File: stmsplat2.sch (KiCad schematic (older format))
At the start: 97 parts, among them J1 C11_2X36, J10 Conn_01x03_Male, J11 Conn_01x02_Male, J12 Conn_01x04_Male, J13 Conn_01x04_Male, J14 Conn_01x02, J15 Conn_01x02, J16 Screw_Terminal_01x03, J17 Screw_Terminal_01x02, J2 C12_2X36, J3 Conn_01x04_Male, J4 Conn_01x04_Male, J5 Conn_Coaxial, J6 Conn_01x06, J7 Conn_01x04_Male, J8 Conn_01x04_Male, J9 Conn_01x03_Male, Q1 BSS138LT1G, U1 ublox_chinese_PCB_module, U10 XCVR_E30-400M20S, U2 ESP-C3-13U, U3 SST25VF032B, U4 48L512-48LM01, U5 Opamp_Quad_MCP6024, U6 E180-ZG120A, U7 AZ1084C, U8 MCP6S93-X_UN, U9 DS2485

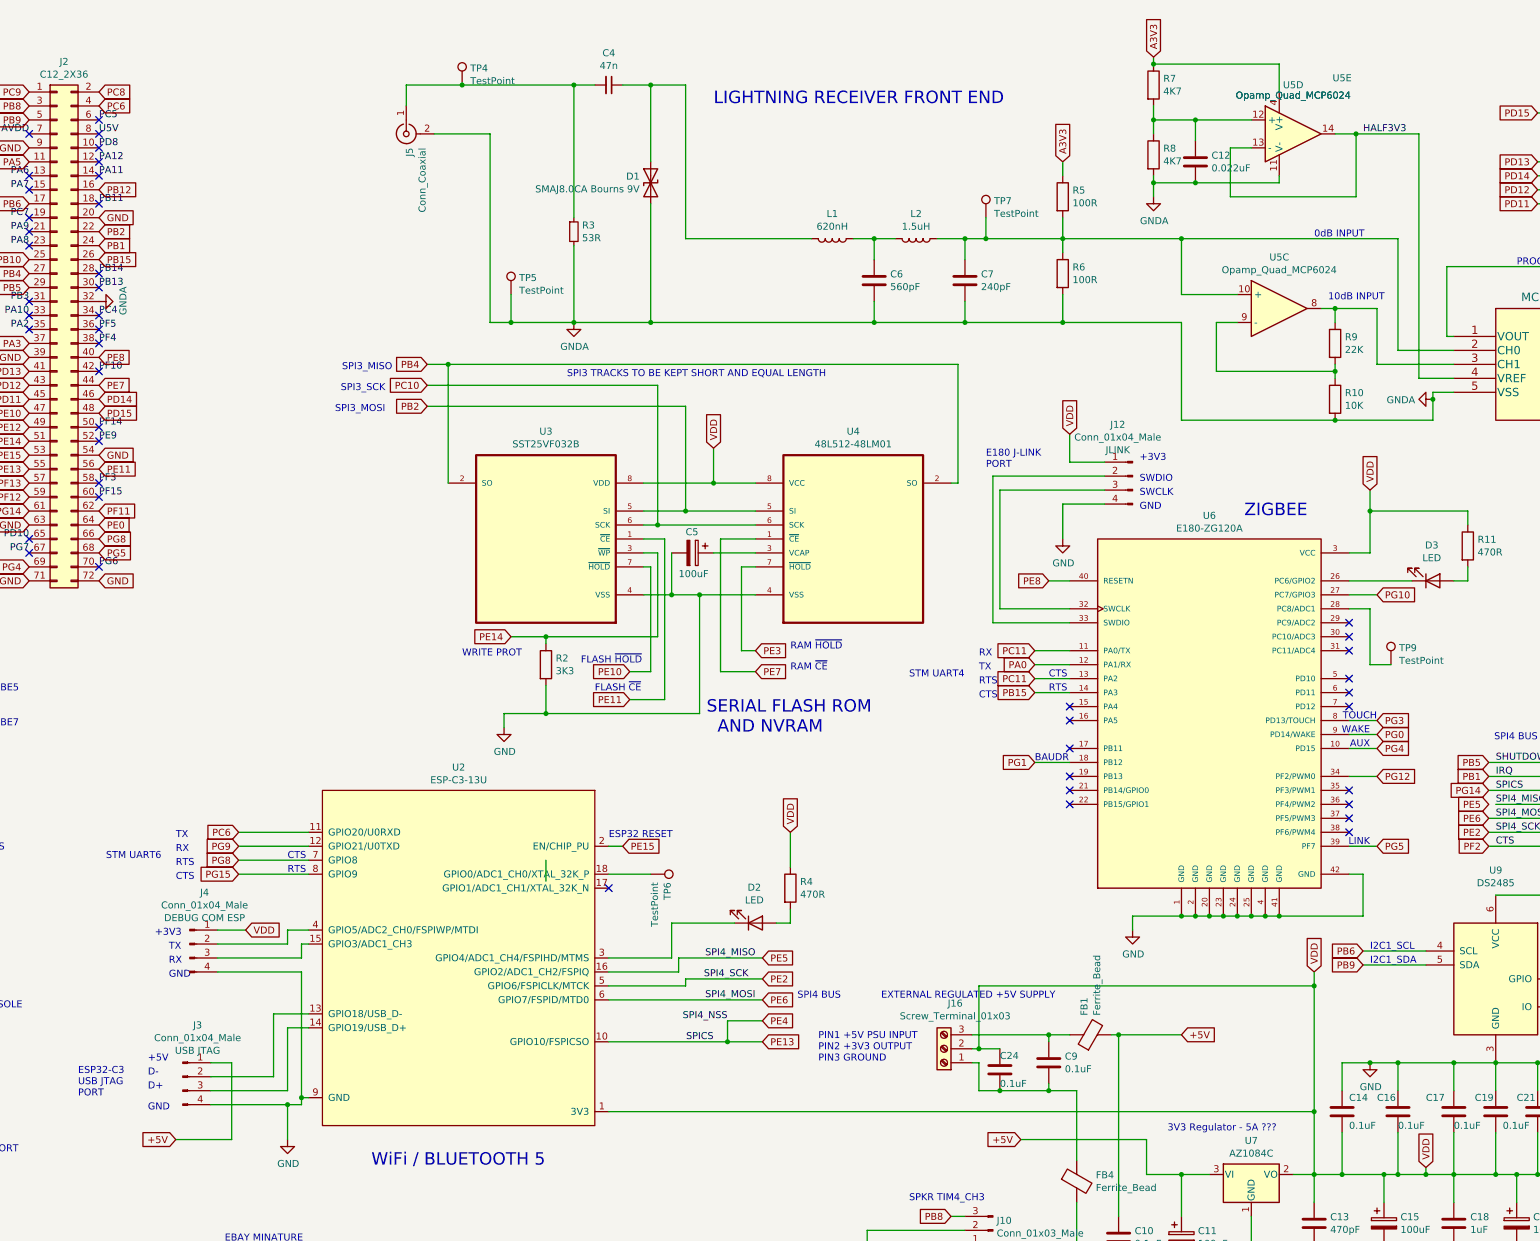
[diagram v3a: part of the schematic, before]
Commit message: 0 ERC - modified custom lib to clarify pin types
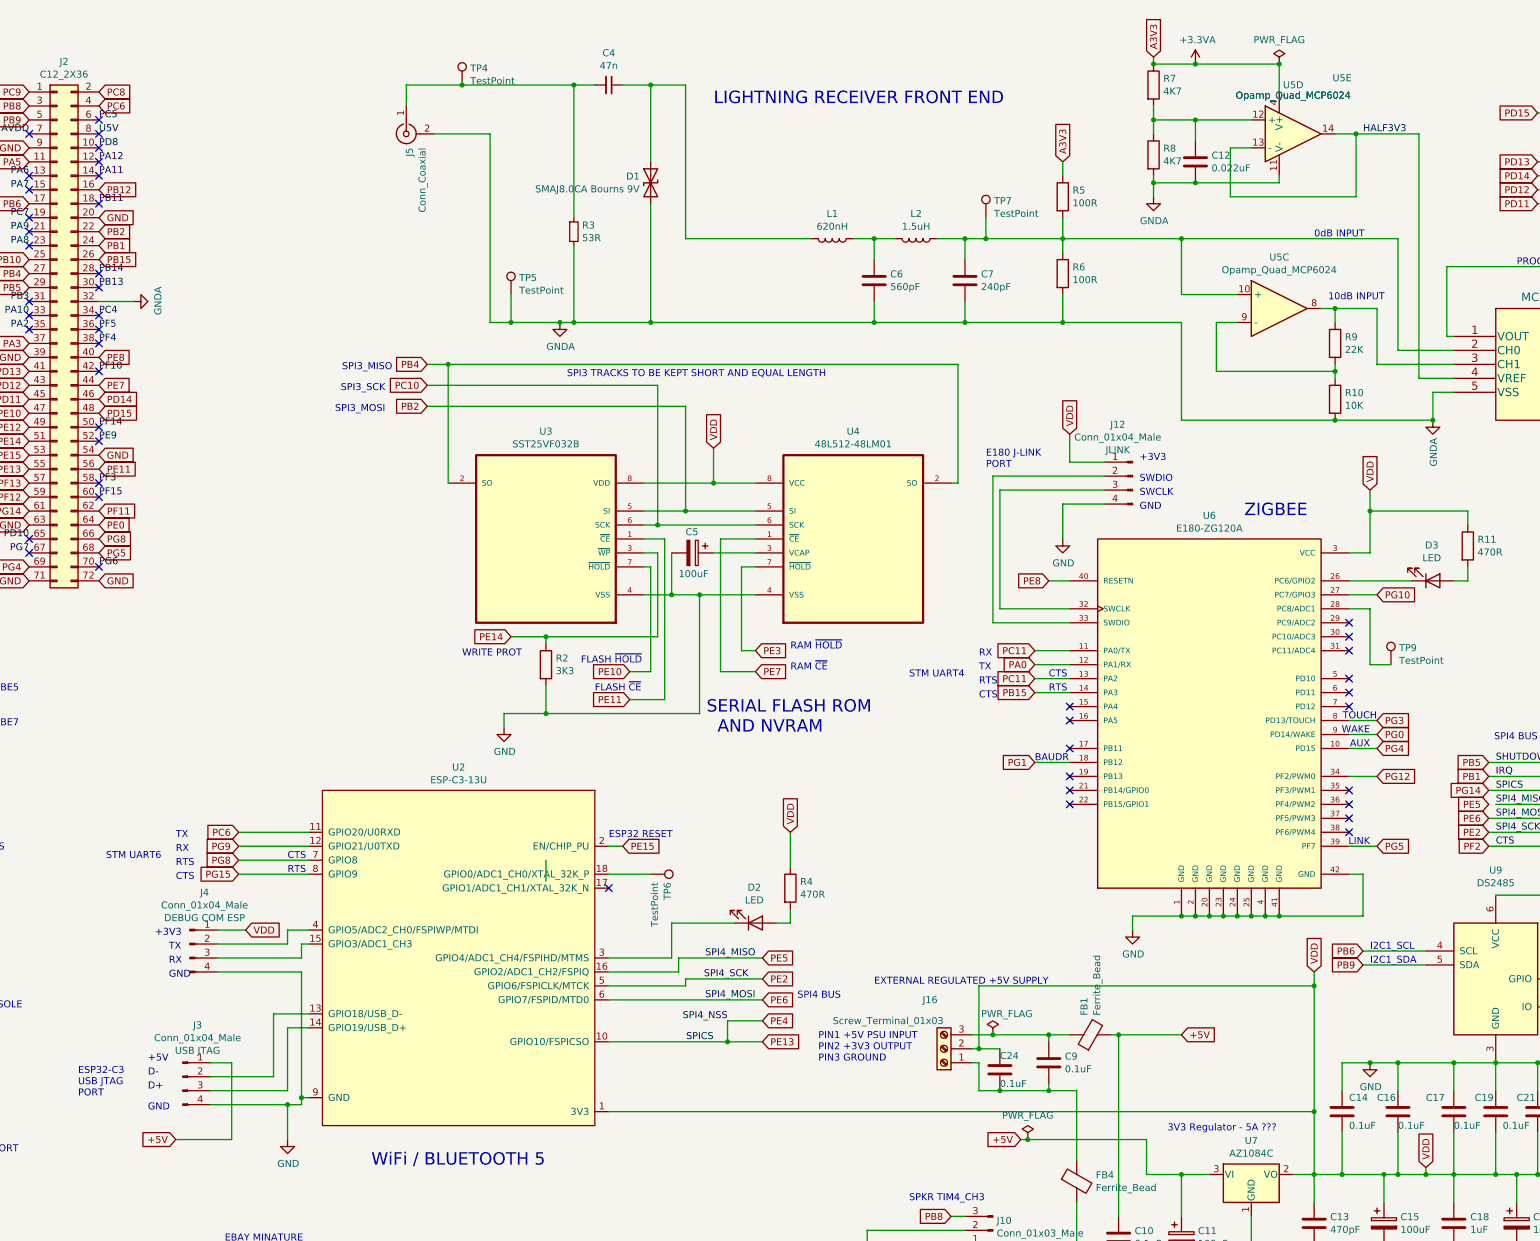
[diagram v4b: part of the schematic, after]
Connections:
- net A3V3 renamed +3.3VA
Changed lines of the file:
@@
 Connection ~ 6950 2650
-Wire Wire Line
-	6400 2650 6950 2650
-Connection ~ 6400 2650
 Wire Wire Line
 	6400 950  6400 1900
@@
 Connection ~ 5950 2650
 Wire Wire Line
-	5950 2650 6400 2650
+	5950 2650 6300 2650
 Wire Wire Line
 	12700 3150 12550 3150
@@
 Wire Wire Line
 	11250 9050 11250 9450
-Text Notes 8600 7500 0    50   ~ 0
+Text Notes 8550 7400 0    50   ~ 0
 EXTERNAL REGULATED +5V SUPPLY
 $Comp
@@
 $EndComp
 Wire Wire Line
-	10550 800  11450 800
+	10550 800  10850 800
 Wire Wire Line
 	11450 800  11450 1000
@@
 U 1 1 622C2AE8
 P 9050 7850
-F 0 "J16" H 8970 7525 50  0000 C CNN
-F 1 "Screw_Terminal_01x03" H 8970 7616 50  0000 C CNN
+F 0 "J16" H 9150 7500 50  0000 C CNN
+F 1 "Screw_Terminal_01x03" H 9450 7650 50  0000 C CNN
 F 2 "TerminalBlock:TerminalBlock_Altech_AK300-3_P5.00mm" H 9050 7850 50  0001 C CNN
 F 3 "~" H 9050 7850 50  0001 C CNN
@@
 $EndComp
 Wire Wire Line
-	9250 7750 9800 7750
+	9250 7750 9400 7750
 Wire Wire Line
 	9250 7950 9300 7950
@@
 	10300 7750 10750 7750
 Wire Wire Line
-	10500 8500 9600 8500
+	10500 8500 9650 8500
 $Comp
 L Connector:Conn_01x04_Male J13
@@
 L power:GNDA #PWR0106
 U 1 1 6451C4EF
-P 12550 3200
-F 0 "#PWR0106" H 12550 2950 50  0001 C CNN
-F 1 "GNDA" V 12555 3073 50  0000 R CNN
-F 2 "" H 12550 3200 50  0001 C CNN
-F 3 "" H 12550 3200 50  0001 C CNN
-	1    12550 3200
-	0    1    1    0
-$EndComp
-Wire Wire Line
-	12550 3150 12550 3200
-Connection ~ 12550 3200
-Wire Wire Line
-	12550 3200 12550 3350
+P 12550 3350
+F 0 "#PWR0106" H 12550 3100 50  0001 C CNN
+F 1 "GNDA" V 12555 3223 50  0000 R CNN
+F 2 "" H 12550 3350 50  0001 C CNN
+F 3 "" H 12550 3350 50  0001 C CNN
+	1    12550 3350
+	1    0    0    -1
+$EndComp
 $Comp
 L power:GNDA #PWR0107
 U 1 1 6466C53B
-P 6400 2650
-F 0 "#PWR0107" H 6400 2400 50  0001 C CNN
-F 1 "GNDA" H 6405 2477 50  0000 C CNN
-F 2 "" H 6400 2650 50  0001 C CNN
-F 3 "" H 6400 2650 50  0001 C CNN
-	1    6400 2650
+P 6300 2650
+F 0 "#PWR0107" H 6300 2400 50  0001 C CNN
+F 1 "GNDA" H 6305 2477 50  0000 C CNN
+F 2 "" H 6300 2650 50  0001 C CNN
+F 3 "" H 6300 2650 50  0001 C CNN
+	1    6300 2650
 	1    0    0    -1
 $EndComp
@@
 L power:GNDA #PWR0109
 U 1 1 648B7644
-P 3000 2500
-F 0 "#PWR0109" H 3000 2250 50  0001 C CNN
-F 1 "GNDA" H 3005 2327 50  0000 C CNN
-F 2 "" H 3000 2500 50  0001 C CNN
-F 3 "" H 3000 2500 50  0001 C CNN
-	1    3000 2500
+P 3250 2500
+F 0 "#PWR0109" H 3250 2250 50  0001 C CNN
+F 1 "GNDA" H 3255 2327 50  0000 C CNN
+F 2 "" H 3250 2500 50  0001 C CNN
+F 3 "" H 3250 2500 50  0001 C CNN
+	1    3250 2500
 	0    -1   -1   0
 $EndComp
@@
 Text GLabel 1650 1200 2    50   Input ~ 0
 +5V
+$Comp
+L power:PWR_FLAG #FLG0101
+U 1 1 65260660
+P 9400 7750
+F 0 "#FLG0101" H 9400 7825 50  0001 C CNN
+F 1 "PWR_FLAG" H 9500 7900 50  0000 C CNN
+F 2 "" H 9400 7750 50  0001 C CNN
+F 3 "~" H 9400 7750 50  0001 C CNN
+	1    9400 7750
+	1    0    0    -1
+$EndComp
+$Comp
+L power:+3.3VA #PWR0110
+U 1 1 652B4945
+P 10850 800
+F 0 "#PWR0110" H 10850 650 50  0001 C CNN
+F 1 "+3.3VA" H 10865 973 50  0000 C CNN
+F 2 "" H 10850 800 50  0001 C CNN
+F 3 "" H 10850 800 50  0001 C CNN
+	1    10850 800
+	1    0    0    -1
+$EndComp
+Connection ~ 10850 800
+Wire Wire Line
+	10850 800  11450 800
+Connection ~ 9400 7750
+Wire Wire Line
+	9400 7750 9800 7750
+Wire Wire Line
+	3250 2500 3000 2500
+Connection ~ 12550 3350
+Wire Wire Line
+	12550 3150 12550 3350
+Connection ~ 6300 2650
+Wire Wire Line
+	6300 2650 6400 2650
+Connection ~ 6400 2650
+Wire Wire Line
+	6400 2650 6950 2650
+$Comp
+L power:PWR_FLAG #FLG0102
+U 1 1 65603B28
+P 9650 8500
+F 0 "#FLG0102" H 9650 8575 50  0001 C CNN
+F 1 "PWR_FLAG" H 9650 8673 50  0000 C CNN
+F 2 "" H 9650 8500 50  0001 C CNN
+F 3 "~" H 9650 8500 50  0001 C CNN
+	1    9650 8500
+	1    0    0    -1
+$EndComp
+Connection ~ 9650 8500
+Wire Wire Line
+	9650 8500 9600 8500
+$Comp
+L power:PWR_FLAG #FLG0103
+U 1 1 656049AA
+P 11450 800
+F 0 "#FLG0103" H 11450 875 50  0001 C CNN
+F 1 "PWR_FLAG" H 11450 973 50  0000 C CNN
+F 2 "" H 11450 800 50  0001 C CNN
+F 3 "~" H 11450 800 50  0001 C CNN
+	1    11450 800
+	1    0    0    -1
+$EndComp
+Connection ~ 11450 800
 $EndSCHEMATC

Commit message: Rejigged library
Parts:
- U1: symbol stmsplat2-rescue:ublox_SAM-M8Q-splatsyms-stmsplat1-rescue-stmsplat2-rescue -> stmsplat2-custom:ublox_SAM-M8Q
- U10: symbol stmsplat2-rescue:XCVR_E30-400M20S-splatlib -> stmsplat2-custom:XCVR_E30-400M20S
- U2: symbol stmsplat2-rescue:ESP32-C3-13-Espressif -> stmsplat2-custom:ESP32-C3-13-Espressif
- U3: symbol stmsplat2-rescue:SST25VF032B-splatlib -> stmsplat2-custom:SST25VF032B
- U4: symbol stmsplat2-rescue:48L512-48LM01-splatlib -> stmsplat2-custom:48L512-48LM01
- U6: symbol stmsplat2-rescue:E180-ZG120A-splatlib -> stmsplat2-custom:E180-ZG120A
- U7: symbol stmsplat2-rescue:AZ1084C-splatlib -> stmsplat2-custom:AZ1084C
- U8: symbol stmsplat2-rescue:MCP6S93-X_UN-splatsyms -> stmsplat2-custom:MCP6S93-X_UN
- U9: symbol stmsplat2-rescue:DS2485-splatlib -> stmsplat2-custom:DS2485
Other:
- note added: "VER 0.06: ALMOST FROZEN - Use custom library"
- note removed: "VER 0.05: ALMOST FROZEN - ERC Checks"
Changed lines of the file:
@@
 Connection ~ 14150 6750
 $Comp
-L stmsplat2-rescue:DS2485-splatlib U9
+L stmsplat2-custom:DS2485 U9
 U 1 1 61A5CBC2
 P 12750 6850
@@
 UART 5
 $Comp
-L stmsplat2-rescue:ESP32-C3-13-Espressif U2
+L stmsplat2-custom:ESP32-C3-13-Espressif U2
 U 1 1 6186BFAC
 P 5600 7250
@@
 	12650 2750 12700 2750
 $Comp
-L stmsplat2-rescue:MCP6S93-X_UN-splatsyms U8
+L stmsplat2-custom:MCP6S93-X_UN U8
 U 1 1 5BD7F0EC
 P 12700 2750
@@
 	6400 950  6400 1900
 $Comp
-L stmsplat2-rescue:XCVR_E30-400M20S-splatlib U10
+L stmsplat2-custom:XCVR_E30-400M20S U10
 U 1 1 61888ACD
 P 14300 5350
@@
 $EndComp
 $Comp
-L stmsplat2-rescue:48L512-48LM01-splatlib U4
+L stmsplat2-custom:48L512-48LM01 U4
 U 1 1 618C0AC4
 P 8400 4100
@@
 $EndComp
 $Comp
-L stmsplat2-rescue:SST25VF032B-splatlib U3
+L stmsplat2-custom:SST25VF032B U3
 U 1 1 618C0BE9
 P 6200 4100
@@
 	2500 9250 3650 9250
 $Comp
-L stmsplat2-rescue:ublox_SAM-M8Q-splatsyms-stmsplat1-rescue-stmsplat2-rescue U1
+L stmsplat2-custom:ublox_SAM-M8Q U1
 U 1 1 5BD908A5
 P 3750 10100
@@
 	9950 5800 9700 5800
 $Comp
-L stmsplat2-rescue:E180-ZG120A-splatlib U6
+L stmsplat2-custom:E180-ZG120A U6
 U 1 1 61E29CE2
 P 10950 5400
@@
 WRITE PROT
 $Comp
-L stmsplat2-rescue:AZ1084C-splatlib U7
+L stmsplat2-custom:AZ1084C U7
 U 1 1 6193E391
 P 11250 8750
@@
 SERIAL FLASH ROM\n  AND NVRAM
 Text Notes 12200 10300 0    89   Italic 0
-VER 0.05: ALMOST FROZEN - ERC Checks
+VER 0.06: ALMOST FROZEN - Use custom library
 $Comp
 L Connector_Generic:Conn_01x02 J14

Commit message: Corrected typo
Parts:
- U2: footprint spatboard:ESP-C3-13 -> ESP-C3-13
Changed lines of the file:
@@
 F 0 "U2" H 5625 8665 50  0000 C CNN
 F 1 "ESP-C3-13U" H 5625 8574 50  0000 C CNN
-F 2 "spatboard:ESP-C3-13" H 5600 5950 50  0001 C CNN
+F 2 "ESP-C3-13" H 5600 5950 50  0001 C CNN
 F 3 "https://docs.ai-thinker.com/_media/esp32/docs/esp-c3-13_specification.pdf" H 3150 5950 50  0001 C CNN
 	1    5600 7250

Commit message: Removed references to spatboard
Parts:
- J12, J3, J4, J7, J8: footprint spatboard:PinHeader_1x04_P2.54mm_Vertical -> PinHeader_1x04_P2.54mm_Vertical
- U1: footprint spatboard:NEO7_GPS_MODULE -> NEO7_GPS_MODULE
- U10: footprint spatboard:XCVR_E30-400M20S -> XCVR_E30-400M20S
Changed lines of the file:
@@
 F 0 "J8" H 7456 10619 50  0000 C CNN
 F 1 "Conn_01x04_Male" H 7456 10528 50  0000 C CNN
-F 2 "spatboard:PinHeader_1x04_P2.54mm_Vertical" H 7350 10250 50  0001 C CNN
+F 2 "PinHeader_1x04_P2.54mm_Vertical" H 7350 10250 50  0001 C CNN
 F 3 "~" H 7350 10250 50  0001 C CNN
 F 4 "NEXTION LCD" H 7456 10437 50  0000 C CNN "DESC"
@@
 F 0 "J7" H 1156 7919 50  0000 C CNN
 F 1 "Conn_01x04_Male" H 1156 7828 50  0000 C CNN
-F 2 "spatboard:PinHeader_1x04_P2.54mm_Vertical" H 1050 7550 50  0001 C CNN
+F 2 "PinHeader_1x04_P2.54mm_Vertical" H 1050 7550 50  0001 C CNN
 F 3 "~" H 1050 7550 50  0001 C CNN
 F 4 "DEBUG COM2" H 1156 7737 50  0000 C CNN "DESC"
@@
 F 0 "J3" H 3706 8419 50  0000 C CNN
 F 1 "Conn_01x04_Male" H 3706 8328 50  0000 C CNN
-F 2 "spatboard:PinHeader_1x04_P2.54mm_Vertical" H 3600 8050 50  0001 C CNN
+F 2 "PinHeader_1x04_P2.54mm_Vertical" H 3600 8050 50  0001 C CNN
 F 3 "~" H 3600 8050 50  0001 C CNN
 F 4 "USB JTAG" H 3706 8237 50  0000 C CNN "DESC"
@@
 F 0 "U10" H 14350 6515 50  0000 C CNN
 F 1 "XCVR_E30-400M20S" H 14350 6424 50  0000 C CNN
-F 2 "spatboard:XCVR_E30-400M20S" H 14300 4100 50  0001 C CNN
+F 2 "XCVR_E30-400M20S" H 14300 4100 50  0001 C CNN
 F 3 "" H 14450 4100 50  0001 C CNN
 	1    14300 5350
@@
 F 0 "J4" H 3756 7469 50  0000 C CNN
 F 1 "Conn_01x04_Male" H 3756 7378 50  0000 C CNN
-F 2 "spatboard:PinHeader_1x04_P2.54mm_Vertical" H 3650 7100 50  0001 C CNN
+F 2 "PinHeader_1x04_P2.54mm_Vertical" H 3650 7100 50  0001 C CNN
 F 3 "~" H 3650 7100 50  0001 C CNN
 F 4 "DEBUG COM ESP" H 3756 7287 50  0000 C CNN "DESC"
@@
 F 0 "U1" H 3750 10778 50  0000 C CNN
 F 1 "ublox_chinese_PCB_module" H 3750 10687 50  0000 C CNN
-F 2 "spatboard:NEO7_GPS_MODULE" H 3750 10000 50  0001 C CNN
+F 2 "NEO7_GPS_MODULE" H 3750 10000 50  0001 C CNN
 F 3 "" H 3750 10100 50  0001 C CNN
 F 4 "M20-7890546" H 3750 10100 50  0001 C CNN "RS Components"
@@
 F 0 "J12" H 10506 4119 50  0000 C CNN
 F 1 "Conn_01x04_Male" H 10506 4028 50  0000 C CNN
-F 2 "spatboard:PinHeader_1x04_P2.54mm_Vertical" H 10400 3750 50  0001 C CNN
+F 2 "PinHeader_1x04_P2.54mm_Vertical" H 10400 3750 50  0001 C CNN
 F 3 "~" H 10400 3750 50  0001 C CNN
 F 4 "JLINK" H 10506 3937 50  0000 C CNN "DESC"
